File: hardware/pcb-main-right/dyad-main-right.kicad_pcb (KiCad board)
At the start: 2 copper layers, 167.2 x 120.7 mm, 148 parts, among them SW1 SW_Push, SW10 SW_Push, SW11 SW_Push, SW12 SW_Push, SW13 SW_Push, SW14 SW_Push, SW15 SW_Push, SW16 SW_Push, SW17 SW_Push, SW18 SW_Push, SW19 SW_Push, SW2 SW_Push, SW20 SW_Push, SW21 SW_Push, SW22 SW_Push, SW23 SW_Push, SW24 SW_Push, SW25 SW_Push, SW26 SW_Push, SW27 SW_Push, SW28 SW_Push, SW29 SW_Push, SW3 SW_Push, SW30 SW_Push, SW31 SW_Push, SW32 SW_Push, SW33 SW_Push, SW34 SW_Push, SW35 SW_Push, SW36 SW_Push, SW37 SW_Push, SW4 SW_Push, SW5 SW_Push, SW6 SW_Push, SW7 SW_Push, SW8 SW_Push, SW9 SW_Push

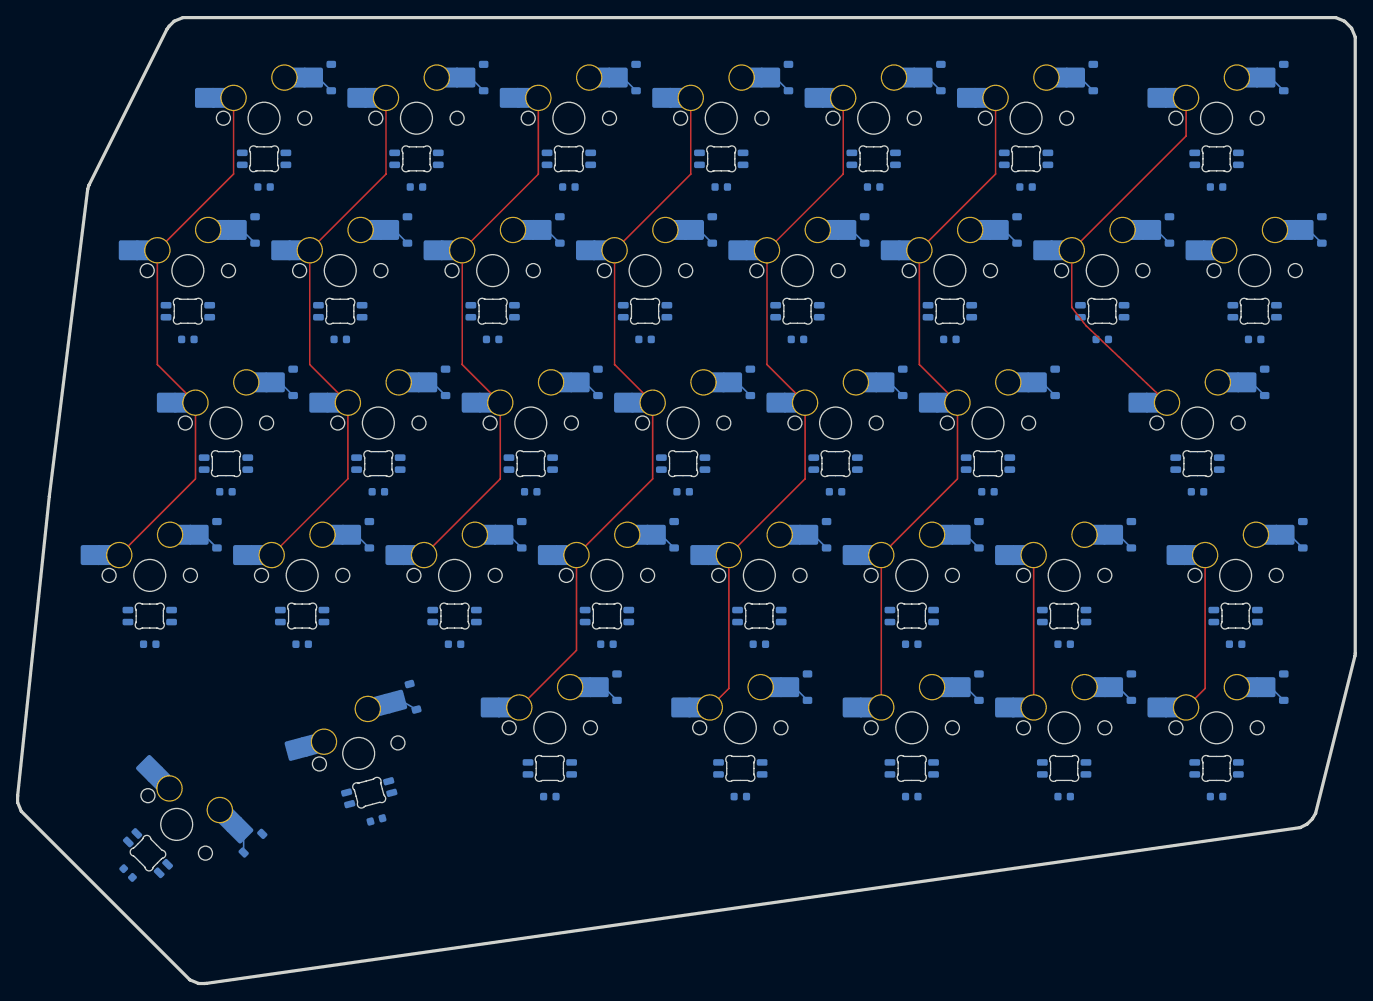
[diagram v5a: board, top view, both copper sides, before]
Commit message: Restore the hand-drawn serpentine LED chain for the right half
I regenerated the right half without checking whether its schematics held
work that was not yet committed, and overwrote a hand-laid serpentine LED
chain. Recovered from hardware/pcb-main-right/.history, KiCad's own version
history repo, at its "SCH Save" commit a7ba379 (2026-09-15 12:59).

The led-chain sheet is byte-identical to that save: 74 symbols, 16 of them
rotated 180 degrees for the alternating rows, with every symbol repositioned
into serpentine order. All 272 wires differ from the generated version, so
this was a full re-layout rather than a rewire.

That history commit happens to postdate 2826d7a, so the bottom-row column
remap and both copper pours came back with it. The only thing missing was
the footprint linking from 2acfb55, re-applied here by calling
_link_footprints_to_symbols directly -- no kbplacer run, so nothing was
regenerated. 148/148 footprints linked.

The board still carries the old sequential chain, which is what the 31
parity findings say:

  Pad net (Net-(LEDn-DOUT)) doesn't match net given by schematic
  (Net-(LEDn-DIN))

That is the serpentine waiting to be pushed with Update PCB from Schematic,
which the footprint links now make possible. The 7 clearance and 7
solder_mask_bridge errors come from the same divergence and should go with it.

Co-Authored-By: Claude Opus 5 <noreply@anthropic.com>
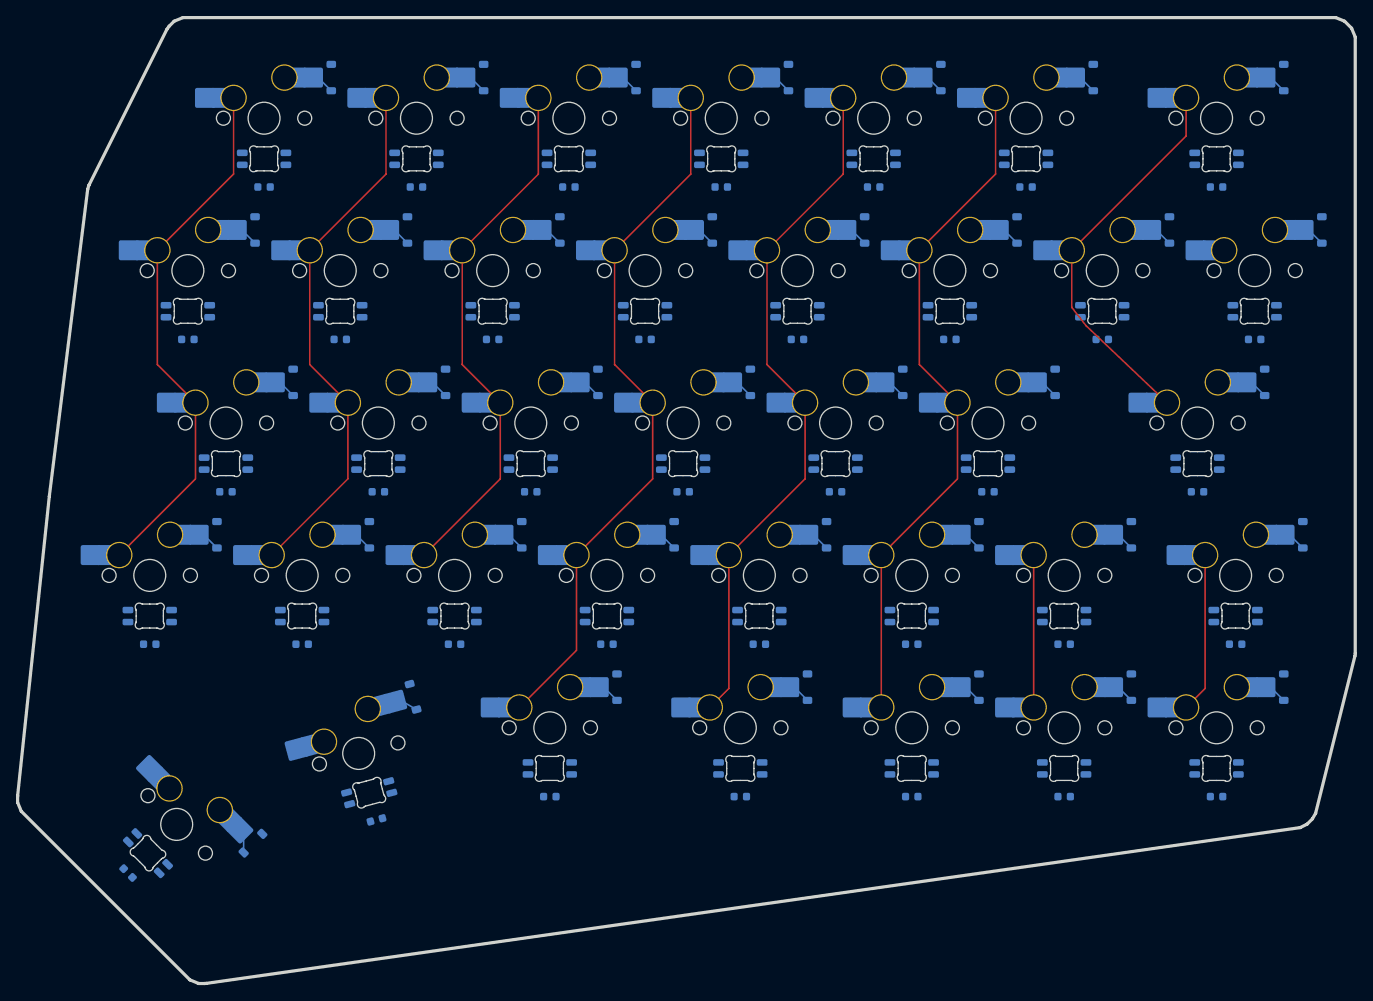
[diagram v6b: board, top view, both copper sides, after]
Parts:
- turned LED1 to 0 degrees
- turned LED16 to 0 degrees
- turned LED17 to 0 degrees
- turned LED18 to 0 degrees
- turned LED19 to 0 degrees
- turned LED2 to 0 degrees
- turned LED20 to 0 degrees
- turned LED21 to 0 degrees
- turned LED22 to 0 degrees
- turned LED3 to 0 degrees
- turned LED31 to -45 degrees
- turned LED32 to 15 degrees
- turned LED33 to 0 degrees
- turned LED34 to 0 degrees
- turned LED35 to 0 degrees
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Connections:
- LED11 pad 2: Net-(LED10-DOUT) -> Net-(LED11-DIN)
- LED11 pad 4: Net-(LED11-DOUT) -> Net-(LED10-DIN)
- LED12 pad 2: Net-(LED11-DOUT) -> Net-(LED12-DIN)
- LED12 pad 4: Net-(LED12-DOUT) -> Net-(LED11-DIN)
- LED13 pad 2: Net-(LED12-DOUT) -> Net-(LED13-DIN)
- LED13 pad 4: Net-(LED13-DOUT) -> Net-(LED12-DIN)
- LED14 pad 2: Net-(LED13-DOUT) -> Net-(LED14-DIN)
- LED14 pad 4: Net-(LED14-DOUT) -> Net-(LED13-DIN)
- LED15 pad 2: Net-(LED14-DOUT) -> Net-(LED15-DIN)
- LED15 pad 4: Net-(LED15-DOUT) -> Net-(LED14-DIN)
- LED16 pad 2: Net-(LED15-DOUT) -> Net-(LED16-DIN)
- LED23 pad 2: Net-(LED22-DOUT) -> Net-(LED23-DIN)
- LED24 pad 2: Net-(LED23-DOUT) -> Net-(LED24-DIN)
- LED24 pad 4: Net-(LED24-DOUT) -> Net-(LED23-DIN)
- LED25 pad 2: Net-(LED24-DOUT) -> Net-(LED25-DIN)
- LED25 pad 4: Net-(LED25-DOUT) -> Net-(LED24-DIN)
- LED26 pad 2: Net-(LED25-DOUT) -> Net-(LED26-DIN)
- LED26 pad 4: Net-(LED26-DOUT) -> Net-(LED25-DIN)
- LED27 pad 2: Net-(LED26-DOUT) -> Net-(LED27-DIN)
- LED27 pad 4: Net-(LED27-DOUT) -> Net-(LED26-DIN)
- LED28 pad 2: Net-(LED27-DOUT) -> Net-(LED28-DIN)
- LED28 pad 4: Net-(LED28-DOUT) -> Net-(LED27-DIN)
- LED29 pad 2: Net-(LED28-DOUT) -> Net-(LED29-DIN)
- LED29 pad 4: Net-(LED29-DOUT) -> Net-(LED28-DIN)
- LED30 pad 2: Net-(LED29-DOUT) -> Net-(LED22-DOUT)
- LED30 pad 4: Net-(LED30-DOUT) -> Net-(LED29-DIN)
- LED31 pad 2: Net-(LED30-DOUT) -> Net-(LED23-DOUT)
- LED7 pad 4: Net-(LED7-DOUT) -> Net-(LED15-DIN)
- LED8 pad 2: Net-(LED7-DOUT) -> Net-(LED8-DIN)
- LED8 pad 4: Net-(LED8-DOUT) -> Net-(LED16-DIN)
- LED9 pad 2: Net-(LED8-DOUT) -> Net-(LED10-DOUT)
- LED9 pad 4: Net-(LED10-DIN) -> Net-(LED8-DIN)

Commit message: Right half fully routed: zero unconnected
413 segments and 37 vias close every connection on main-right. The VCC vias
bridge the F.Cu pour to the B.Cu-only pads, one per LED/capacitor pair, which
is what the pour needed to stop being decorative.

  unconnected   145 -> 0
  parity          0 -> 0
  errors         37 -> 37   (all courtyards_overlap)
  shorts          0

Everything that remains is cosmetic or deliberate:

  132  silk_over_copper      reference designators over pad mask openings
   63  silk_overlap          designators colliding with each other
   37  courtyards_overlap    the diode-under-switch placement, by design
   21  silk_edge_clearance   designators past the board edge

No clearance, hole, edge or connectivity violations of any kind. The stored
zone fill is current -- refilling on a copy reproduces the identical result,
so none of these numbers rest on a stale fill.

main-left is untouched and still unrouted.

Co-Authored-By: Claude Opus 5 <noreply@anthropic.com>
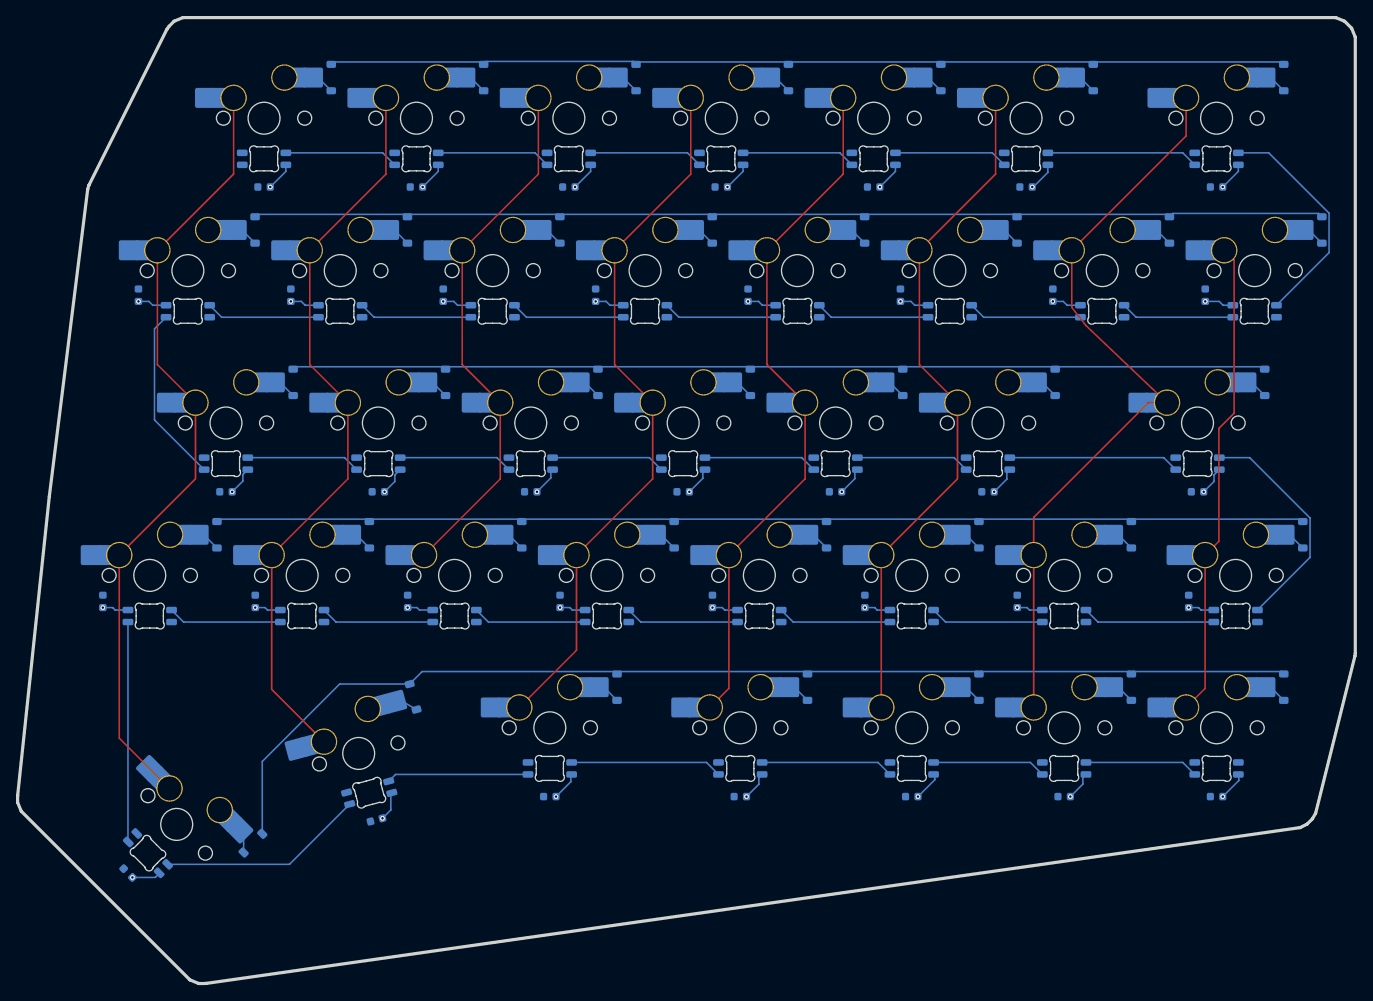
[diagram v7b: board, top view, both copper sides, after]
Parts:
- moved C11 8.29 mm to (98.6, 60.2), turned to 90 degrees
- moved C13 8.29 mm to (136.7, 60.2), turned to 90 degrees
- moved C14 8.29 mm to (155.8, 60.2), turned to 90 degrees
- moved C10 8.29 mm to (79.5, 60.2), turned to 90 degrees
- moved C12 8.29 mm to (117.7, 60.2), turned to 90 degrees
- moved C8 8.29 mm to (41.5, 60.2), turned to 90 degrees
- moved C9 8.29 mm to (60.5, 60.2), turned to 90 degrees
- moved C15 8.29 mm to (174.8, 60.2), turned to 90 degrees
- moved C25 7.94 mm to (75.1, 98.5), turned to 90 degrees
- moved C28 7.94 mm to (132.2, 98.5), turned to 90 degrees
- moved C30 7.94 mm to (172.7, 98.5), turned to 90 degrees
- moved C24 7.94 mm to (56.0, 98.5), turned to 90 degrees
- moved C23 7.94 mm to (37.0, 98.5), turned to 90 degrees
- moved C26 7.94 mm to (94.2, 98.5), turned to 90 degrees
- moved C27 7.94 mm to (113.2, 98.5), turned to 90 degrees
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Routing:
- net ROW4: track 0.00 -> 142.5 mm
- net ROW3: track 0.00 -> 137.5 mm
- net ROW1: track 0.00 -> 135.2 mm
- net VCC: track 0.00 -> 130.8 mm, vias 0 -> 37
- net ROW2: track 0.00 -> 122.9 mm
- net ROW0: track 0.00 -> 120.6 mm
- net COL7: track 20.0 -> 60.1 mm
- net COL0: track 67.0 -> 98.8 mm
- net Net-(LED15-DIN): track 0.00 -> 28.7 mm
- net Net-(LED22-DOUT): track 0.00 -> 28.7 mm
- net Net-(LED23-DOUT): track 0.00 -> 27.5 mm
- net COL6: track 68.0 -> 95.3 mm
- net COL1: track 67.0 -> 93.0 mm
- net Net-(LED31-DOUT): track 0.00 -> 25.9 mm
- net Net-(LED16-DIN): track 0.00 -> 22.2 mm
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
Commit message: Route the FFC connector on the right main PCB
J1 placed on B.Cu at the left edge and hand-routed, 413 -> 544 segments and
37 -> 65 vias. Unconnected stays 0 and schematic parity holds. Track widths
and vias match the rest of the board throughout: 0.2 mm, 0.6/0.3.

Two things were reworked during routing:

  The row order was reversed at the connector, ascending -> descending, to
  stop the five row traces crossing on their run to J1. Schematic and board
  were both updated, so this is the pinout of record now.

  The LED serpentine was re-laid so horizontal links sit on one layer and
  vertical links on the other. Routing the connector had pinched the B.Cu
  GND pour into three pieces -- two bands of roughly 864 and 833 mm^2 fenced
  off from the main pour and left floating, which DRC reported as 2
  unconnected items. No pad was ever stranded, but the layer split restored
  a single pour: 1 island of 13,311 mm^2, unconnected back to 0. Worth
  remembering that F.Cu is the VCC pour here, so a fragmented GND cannot be
  stitched through the other layer -- it has to be solved in B.Cu geometry.

Known remaining, neither a regression:

  One track_dangling, a 0.063 mm ROW4 stub on F.Cu at (61.28, 114.16),
  left over from the reroute. 253 -> 254 violations.

  One schematic_parity, footprint_symbol_field_mismatch on J1's Pinout
  text: the schematic says ROW4..ROW0 and the board still carries the old
  ROW0-4 string. Documentation text only, no nets involved; it clears on
  the next Update PCB from Schematic.

Everything else is unchanged from the documented baseline: 37
courtyards_overlap from the deliberate diode-under-switch placement, and
216 silkscreen findings.

Co-Authored-By: Claude Opus 5 <noreply@anthropic.com>
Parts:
- added J1: HC-FPC-0.5-20P-FH20, dyad:FPC-SMD_20P-P0.50_HC-FPC-0.5-20P-FH20, B.Cu at (37.8, 77.0)
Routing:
- net COL7: track 60.1 -> 205.8 mm, vias 0 -> 1
- net COL6: track 95.3 -> 224.5 mm, vias 0 -> 1
- net COL5: track 86.1 -> 192.5 mm, vias 0 -> 1
- net COL4: track 87.0 -> 174.5 mm, vias 0 -> 1
- net COL3: track 89.0 -> 157.4 mm, vias 0 -> 1
- net ROW0: track 120.6 -> 188.7 mm, vias 0 -> 2
- net COL2: track 67.0 -> 116.4 mm, vias 0 -> 1
- net LEDIN: track 0.00 -> 46.6 mm, vias 0 -> 2
- net ROW1: track 135.2 -> 181.2 mm, vias 0 -> 2
- net ROW4: track 142.5 -> 188.3 mm, vias 0 -> 2
- net ROW2: track 122.9 -> 153.4 mm, vias 0 -> 2
- net COL1: track 93.0 -> 123.5 mm, vias 0 -> 1
- net ROW3: track 137.5 -> 153.7 mm
- net Net-(LED15-DIN): track 28.7 -> 21.9 mm, vias 0 -> 2
- net Net-(LED22-DOUT): track 28.7 -> 22.1 mm, vias 0 -> 2
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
